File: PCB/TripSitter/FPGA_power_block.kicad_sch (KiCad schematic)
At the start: 25 parts, among them U1 XC7A100T-FGG484

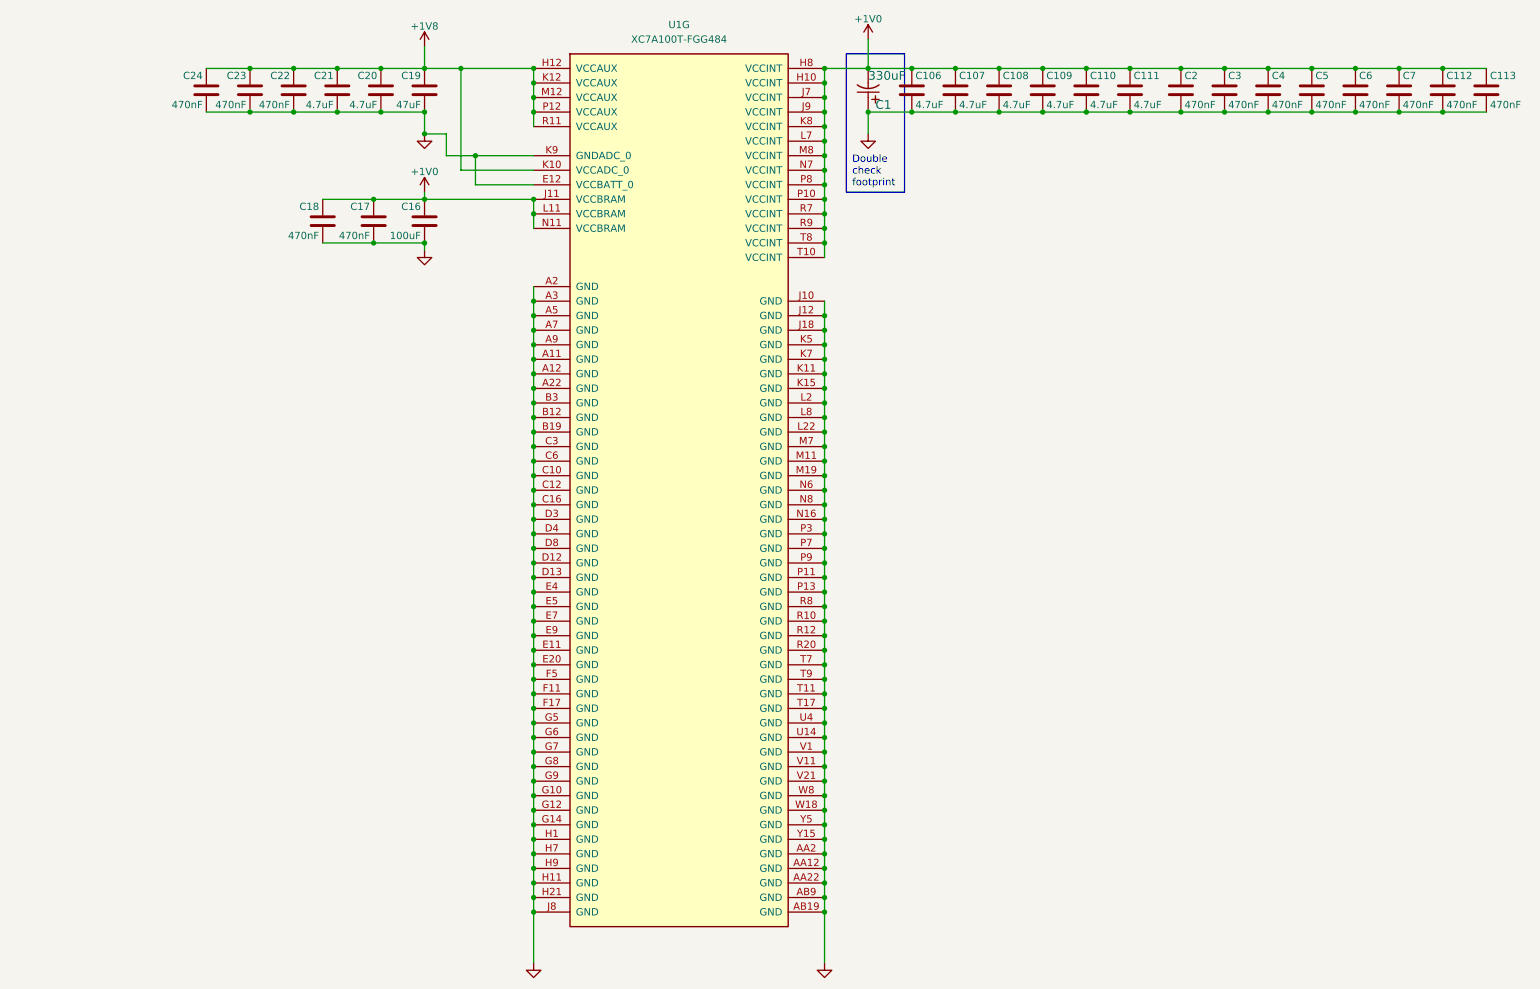
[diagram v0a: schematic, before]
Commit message: pcb: re-structured PCB schematic layout (#17)
Co-authored-by: Sigvart Hovland <sigvart.m@gmail.com>
Co-authored-by: Ida-Sofie Pettersen <idasofie@Ida-Sofies-MacBook-Air.local>
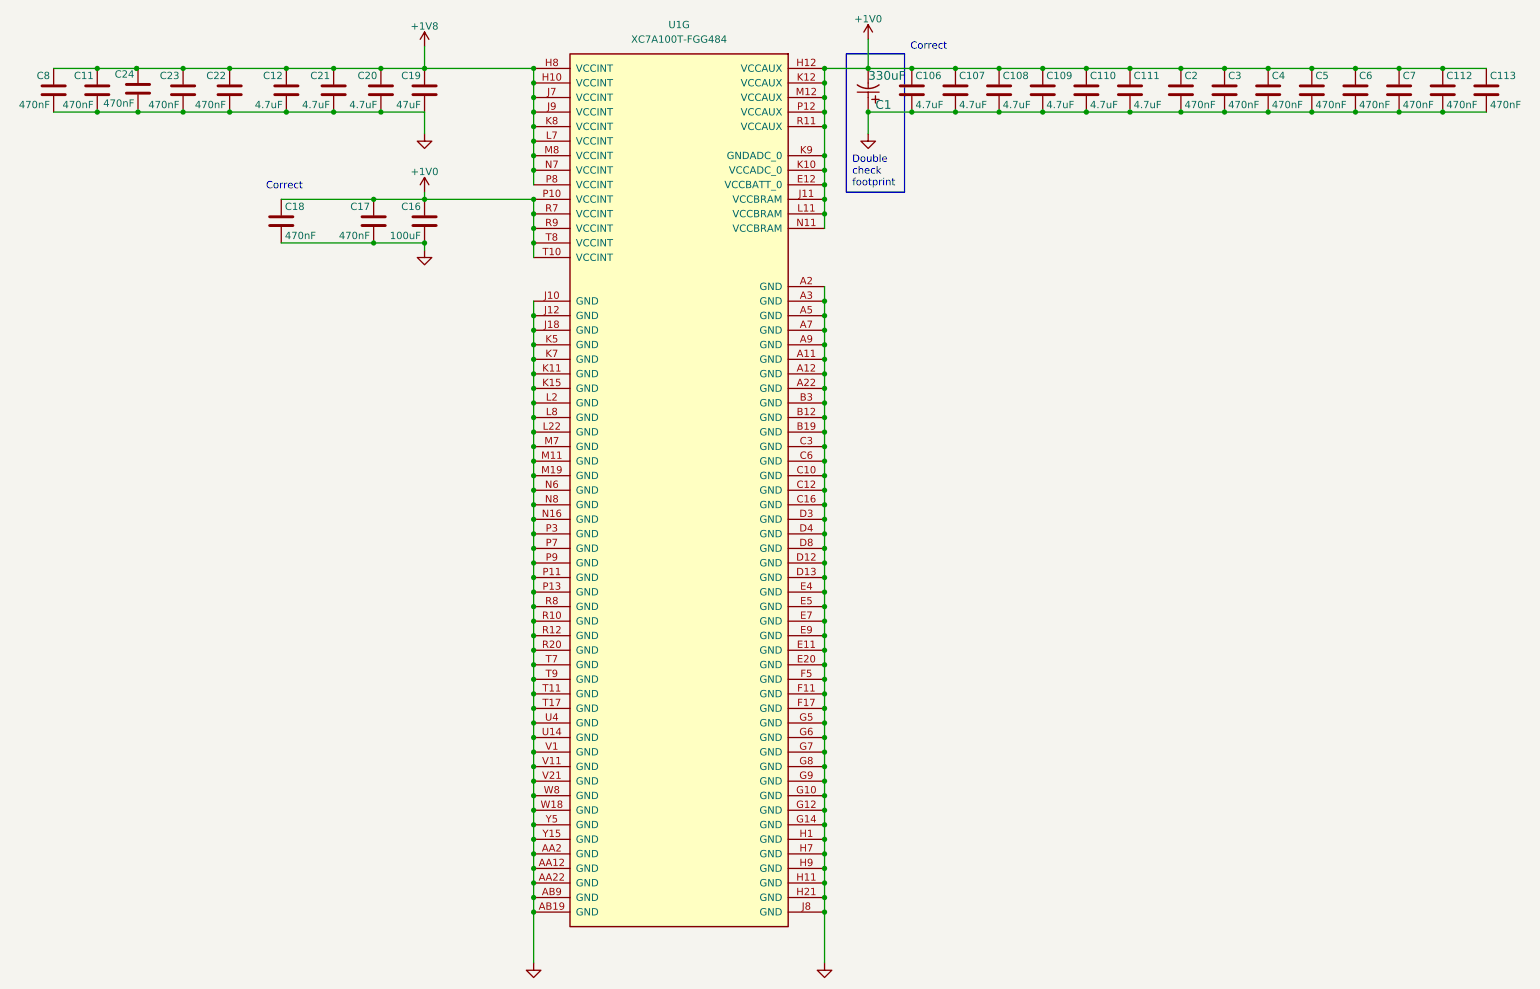
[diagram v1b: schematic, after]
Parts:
- added C11, C8: 470nF, Capacitor_SMD:C_0201_0603Metric_Pad0.64x0.40mm_HandSolder, symbol Device:C
- added C12: 4.7uF, Capacitor_SMD:C_0201_0603Metric_Pad0.64x0.40mm_HandSolder, symbol Device:C
- C106: footprint Capacitor_SMD:C_01005_0402Metric_Pad0.57x0.30mm_HandSolder -> Capacitor_SMD:C_0201_0603Metric_Pad0.64x0.40mm_HandSolder; DK_Detail_Page https://www.digikey.no/no/products/detail/samsung-electro-mechanics/CL05A475KQ5NRNC/3887139 -> https://www.digikey.no/no/products/detail/samsung-electro-mechanics/CL03A475MQ5C65C/16572790
- C107, C108, C109, C110, C111: footprint Capacitor_SMD:C_01005_0402Metric_Pad0.57x0.30mm_HandSolder -> Capacitor_SMD:C_0201_0603Metric_Pad0.64x0.40mm_HandSolder
- C16: footprint Capacitor_SMD:C_1210_3225Metric_Pad1.33x2.70mm_HandSolder -> Capacitor_SMD:C_0805_2012Metric_Pad1.18x1.45mm_HandSolder; Component name CL32A107MPVNNNE -> GRM21BR60G107ME11L; DK_Detail_Page https://www.digikey.no/product-detail/en/samsung-electro-me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 -> https://www.digikey.no/en/products/detail/murata-electronic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
- C19: footprint Capacitor_SMD:C_1210_3225Metric_Pad1.33x2.70mm_HandSolder -> Capacitor_SMD:C_0603_1608Metric_Pad1.08x0.95mm_HandSolder; Component name CL32A476KOJNNNE -> CL10A476MR8NZNE; DK_Detail_Page https://www.digikey.no/product-detail/no/murata-electronics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 -> https://www.digikey.no/no/products/detail/samsung-electro-m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
- C20, C21: footprint Capacitor_SMD:C_0805_2012Metric_Pad1.18x1.45mm_HandSolder -> Capacitor_SMD:C_0201_0603Metric_Pad0.64x0.40mm_HandSolder; Component name C2012X7R1A475K125AC -> CL05A475KQ5NRNC; DK_Detail_Page https://www.digikey.no/product-detail/no/tdk-corporation/C2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 -> https://www.digikey.no/no/products/detail/samsung-electro-m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
- C22: Component name GRM188R71C474KA88D -> CL03A474KQ3NNNH; DK_Detail_Page https://www.digikey.no/product-detail/en/murata-electronics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 -> https://www.digikey.no/en/products/detail/samsung-electro-m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
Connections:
- net +1V0: now also U1.E12 (VCCBATT_0), U1.H12 (VCCAUX), U1.K10 (VCCADC_0), U1.K12 (VCCAUX), U1.K9 (GNDADC_0), U1.M12 (VCCAUX), U1.P12 (VCCAUX), U1.R11 (VCCAUX); no longer U1.H10 (VCCINT), U1.H8 (VCCINT), U1.J7 (VCCINT), U1.J9 (VCCINT), U1.K8 (VCCINT), U1.L7 (VCCINT), U1.M8 (VCCINT), U1.N7 (VCCINT), U1.P8 (VCCINT)
- net +1V8: now also U1.H10 (VCCINT), U1.H8 (VCCINT), U1.J7 (VCCINT), U1.J9 (VCCINT), U1.K8 (VCCINT), U1.L7 (VCCINT), U1.M8 (VCCINT), U1.N7 (VCCINT), U1.P8 (VCCINT), C11.1, C12.1, C8.1; no longer U1.H12 (VCCAUX), U1.K10 (VCCADC_0), U1.K12 (VCCAUX), U1.M12 (VCCAUX), U1.P12 (VCCAUX), U1.R11 (VCCAUX)
- net GND: now also C11.2, C12.2, C8.2; no longer U1.E12 (VCCBATT_0), U1.K9 (GNDADC_0)
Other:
- note added: "Correct"
- moved on the sheet: C18, C22, C23, C24
